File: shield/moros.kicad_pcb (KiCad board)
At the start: 2 copper layers, 48.8 x 18.8 mm, 7 parts, among them U1 ARDUINO_MICRO_SHIELD

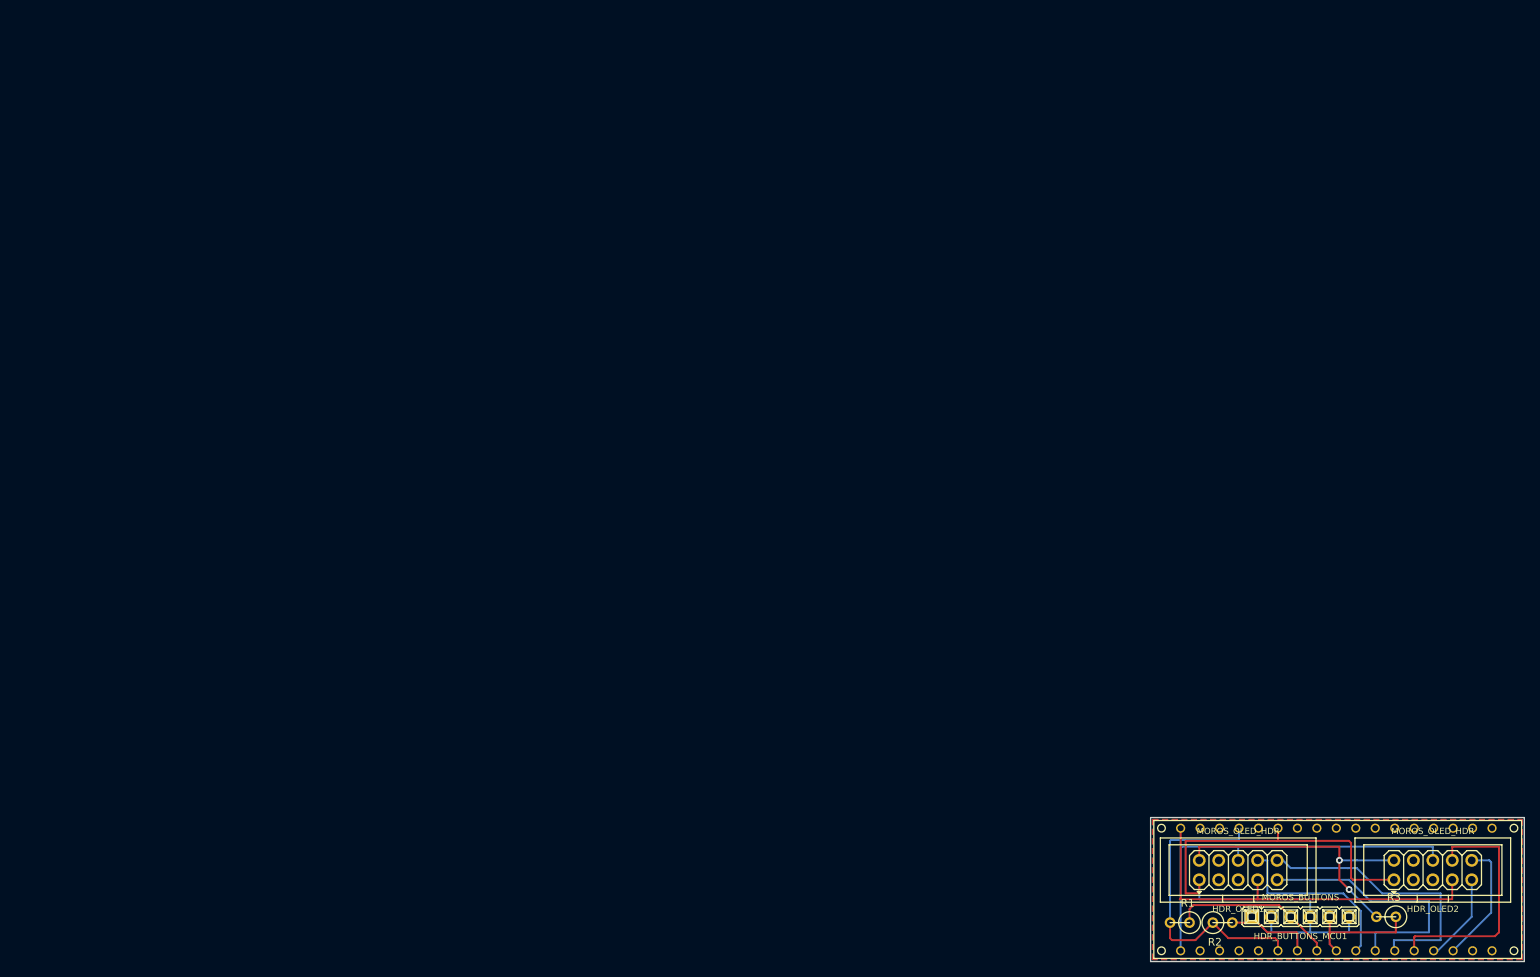
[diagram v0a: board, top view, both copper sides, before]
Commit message: Use new arduino shield template
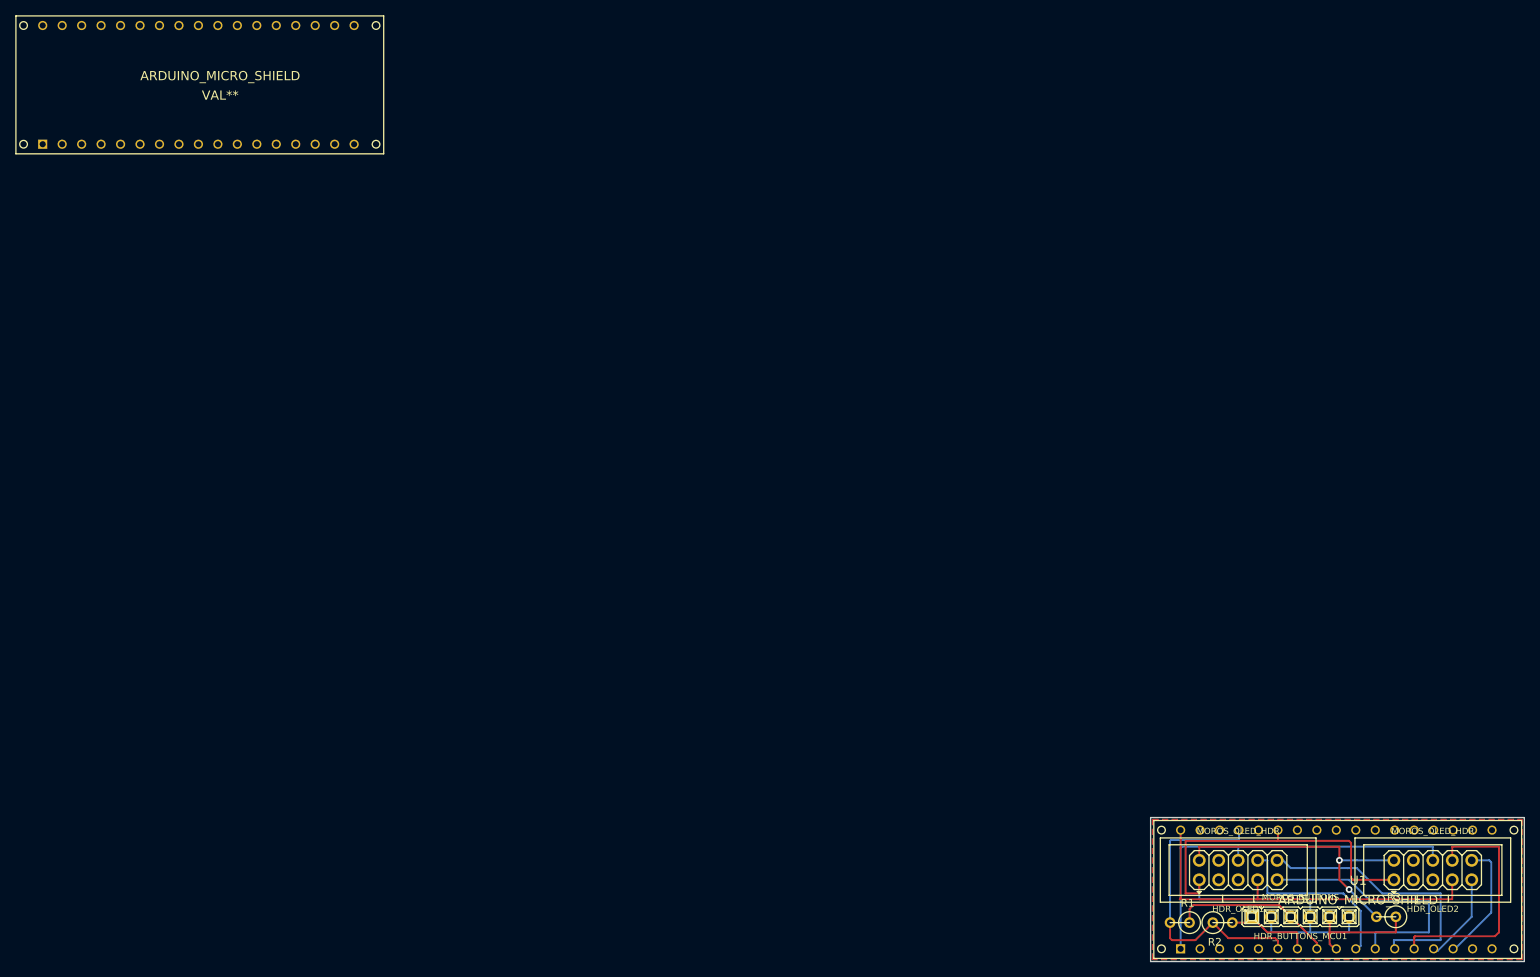
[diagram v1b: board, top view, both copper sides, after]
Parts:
- added ARDUINO_MICRO_SHIELD: VAL**, arduino_micro_shield:ARDUINO_MICRO_SHIELD, F.Cu at (0.00, 0.00)
- U1: footprint micro:ARDUINO_MICRO_SHIELD -> arduino_micro_shield:ARDUINO_MICRO_SHIELD
